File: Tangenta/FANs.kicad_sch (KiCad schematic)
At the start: 8 parts, among them M1 Fan_4pin, M2 Fan_4pin, Q3 BSS138

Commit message: Libraries exported from global to project.
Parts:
- M1, M2: symbol Motor:Fan_4pin -> CholaSymbolsPrjLib:Fan_4pin
- Q3: symbol Transistor_FET:BSS138 -> CholaSymbolsPrjLib:BSS138
- R2: symbol Device:R_Small_US -> CholaSymbolsPrjLib:R_Small_US
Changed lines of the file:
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@@
     (effects (font (size 1.27 1.27)) (justify right))
   )
-  (symbol (lib_id "Device:R_Small_US") (at 127 111.76 180) (unit 1)
+  (symbol (lib_id "CholaSymbolsPrjLib:R_Small_US") (at 127 111.76 180) (unit 1)
     (in_bom yes) (on_board yes) (dnp no)
     (property "Reference" "R2" (at 125.73 110.49 0)
@@
     )
   )
-  (symbol (lib_id "Device:R_Small_US") (at 127 78.105 180) (unit 1)
+  (symbol (lib_id "CholaSymbolsPrjLib:R_Small_US") (at 127 78.105 180) (unit 1)
     (in_bom yes) (on_board yes) (dnp no)
     (property "Reference" "R2" (at 125.73 76.835 0)
@@
     )
   )
-  (symbol (lib_id "Motor:Fan_4pin") (at 181.61 115.57 0) (unit 1)
+  (symbol (lib_id "CholaSymbolsPrjLib:Fan_4pin") (at 181.61 115.57 0) (unit 1)
     (in_bom yes) (on_board yes) (dnp no)
     (property "Reference" "M2" (at 185.42 114.3 0)
@@
     )
   )
-  (symbol (lib_id "Transistor_FET:BSS138") (at 139.7 115.57 270) (unit 1)
+  (symbol (lib_id "CholaSymbolsPrjLib:BSS138") (at 139.7 115.57 270) (unit 1)
     (in_bom yes) (on_board yes) (dnp no)
     (property "Reference" "Q3" (at 142.24 113.03 90)
@@
     )
   )
-  (symbol (lib_id "Device:R_Small_US") (at 153.67 111.76 180) (unit 1)
+  (symbol (lib_id "CholaSymbolsPrjLib:R_Small_US") (at 153.67 111.76 180) (unit 1)
     (in_bom yes) (on_board yes) (dnp no)
     (property "Reference" "R2" (at 152.4 110.49 0)
@@
     )
   )
-  (symbol (lib_id "Device:R_Small_US") (at 153.67 78.105 180) (unit 1)
+  (symbol (lib_id "CholaSymbolsPrjLib:R_Small_US") (at 153.67 78.105 180) (unit 1)
     (in_bom yes) (on_board yes) (dnp no)
     (property "Reference" "R2" (at 152.4 76.835 0)
@@
     )
   )
-  (symbol (lib_id "Motor:Fan_4pin") (at 181.61 81.915 0) (unit 1)
+  (symbol (lib_id "CholaSymbolsPrjLib:Fan_4pin") (at 181.61 81.915 0) (unit 1)
     (in_bom yes) (on_board yes) (dnp no)
     (property "Reference" "M1" (at 185.42 80.645 0)
@@
     )
   )
-  (symbol (lib_id "Transistor_FET:BSS138") (at 139.7 81.915 270) (unit 1)
+  (symbol (lib_id "CholaSymbolsPrjLib:BSS138") (at 139.7 81.915 270) (unit 1)
     (in_bom yes) (on_board yes) (dnp no)
     (property "Reference" "Q3" (at 142.24 79.375 90)

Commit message: initialize branch
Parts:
- renumbered Q3 to Q23, Q3 to Q24, R2 to R204, R2 to R205, R2 to R206, R2 to R207
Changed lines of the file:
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@@
   (symbol (lib_id "CholaSymbolsPrjLib:R_Small_US") (at 127 111.76 180) (unit 1)
     (in_bom yes) (on_board yes) (dnp no)
-    (property "Reference" "R2" (at 125.73 110.49 0)
+    (property "Reference" "R205" (at 125.73 110.49 0)
       (effects (font (size 1.27 1.27)) (justify left))
     )
@@
     (instances
       (project "Tangenta"
-        (path "/358d1bcf-7599-4352-8c4d-baa18a5f09e6/8215796b-9611-4f43-bcc5-319f8414b8a6"
-          (reference "R2") (unit 1)
-        )
-        (path "/358d1bcf-7599-4352-8c4d-baa18a5f09e6/d6c05402-162e-441f-bed8-be7996260fb4"
-          (reference "R18") (unit 1)
-        )
-        (path "/358d1bcf-7599-4352-8c4d-baa18a5f09e6/b1871a4d-6a35-44e2-a9a2-9a4af684371d"
-          (reference "R26") (unit 1)
-        )
-        (path "/358d1bcf-7599-4352-8c4d-baa18a5f09e6/6a8c68b5-4a7d-449e-86f6-34ced6d1cb55"
-          (reference "R41") (unit 1)
-        )
-        (path "/358d1bcf-7599-4352-8c4d-baa18a5f09e6/db297b0b-35f2-4e86-892c-83973f1ac2db"
-          (reference "R41") (unit 1)
-        )
-        (path "/358d1bcf-7599-4352-8c4d-baa18a5f09e6/98e3b24f-9927-4339-b8fd-9deea91a522a"
-          (reference "R158") (unit 1)
-        )
         (path "/358d1bcf-7599-4352-8c4d-baa18a5f09e6/19b4ac3b-c2a1-43b1-8d7b-1ca5ac2c79ee"
           (reference "R205") (unit 1)
@@
   (symbol (lib_id "CholaSymbolsPrjLib:R_Small_US") (at 127 78.105 180) (unit 1)
     (in_bom yes) (on_board yes) (dnp no)
-    (property "Reference" "R2" (at 125.73 76.835 0)
+    (property "Reference" "R204" (at 125.73 76.835 0)
       (effects (font (size 1.27 1.27)) (justify left))
     )
@@
     (instances
       (project "Tangenta"
-        (path "/358d1bcf-7599-4352-8c4d-baa18a5f09e6/8215796b-9611-4f43-bcc5-319f8414b8a6"
-          (reference "R2") (unit 1)
-        )
-        (path "/358d1bcf-7599-4352-8c4d-baa18a5f09e6/d6c05402-162e-441f-bed8-be7996260fb4"
-          (reference "R18") (unit 1)
-        )
-        (path "/358d1bcf-7599-4352-8c4d-baa18a5f09e6/b1871a4d-6a35-44e2-a9a2-9a4af684371d"
-          (reference "R26") (unit 1)
-        )
-        (path "/358d1bcf-7599-4352-8c4d-baa18a5f09e6/6a8c68b5-4a7d-449e-86f6-34ced6d1cb55"
-          (reference "R41") (unit 1)
-        )
-        (path "/358d1bcf-7599-4352-8c4d-baa18a5f09e6/db297b0b-35f2-4e86-892c-83973f1ac2db"
-          (reference "R41") (unit 1)
-        )
-        (path "/358d1bcf-7599-4352-8c4d-baa18a5f09e6/98e3b24f-9927-4339-b8fd-9deea91a522a"
-          (reference "R158") (unit 1)
-        )
         (path "/358d1bcf-7599-4352-8c4d-baa18a5f09e6/19b4ac3b-c2a1-43b1-8d7b-1ca5ac2c79ee"
           (reference "R204") (unit 1)
@@
   (symbol (lib_id "CholaSymbolsPrjLib:BSS138") (at 139.7 115.57 270) (unit 1)
     (in_bom yes) (on_board yes) (dnp no)
-    (property "Reference" "Q3" (at 142.24 113.03 90)
+    (property "Reference" "Q24" (at 142.24 113.03 90)
       (effects (font (size 1.27 1.27)))
     )
@@
     (instances
       (project "Tangenta"
-        (path "/358d1bcf-7599-4352-8c4d-baa18a5f09e6/6a8c68b5-4a7d-449e-86f6-34ced6d1cb55"
-          (reference "Q3") (unit 1)
-        )
-        (path "/358d1bcf-7599-4352-8c4d-baa18a5f09e6/db297b0b-35f2-4e86-892c-83973f1ac2db"
-          (reference "Q5") (unit 1)
-        )
-        (path "/358d1bcf-7599-4352-8c4d-baa18a5f09e6/98e3b24f-9927-4339-b8fd-9deea91a522a"
-          (reference "Q10") (unit 1)
-        )
         (path "/358d1bcf-7599-4352-8c4d-baa18a5f09e6/19b4ac3b-c2a1-43b1-8d7b-1ca5ac2c79ee"
           (reference "Q24") (unit 1)
@@
   (symbol (lib_id "CholaSymbolsPrjLib:R_Small_US") (at 153.67 111.76 180) (unit 1)
     (in_bom yes) (on_board yes) (dnp no)
-    (property "Reference" "R2" (at 152.4 110.49 0)
+    (property "Reference" "R207" (at 152.4 110.49 0)
       (effects (font (size 1.27 1.27)) (justify left))
     )
@@
     (instances
       (project "Tangenta"
-        (path "/358d1bcf-7599-4352-8c4d-baa18a5f09e6/8215796b-9611-4f43-bcc5-319f8414b8a6"
-          (reference "R2") (unit 1)
-        )
-        (path "/358d1bcf-7599-4352-8c4d-baa18a5f09e6/d6c05402-162e-441f-bed8-be7996260fb4"
-          (reference "R18") (unit 1)
-        )
-        (path "/358d1bcf-7599-4352-8c4d-baa18a5f09e6/b1871a4d-6a35-44e2-a9a2-9a4af684371d"
-          (reference "R28") (unit 1)
-        )
-        (path "/358d1bcf-7599-4352-8c4d-baa18a5f09e6/db297b0b-35f2-4e86-892c-83973f1ac2db"
-          (reference "R28") (unit 1)
-        )
-        (path "/358d1bcf-7599-4352-8c4d-baa18a5f09e6/98e3b24f-9927-4339-b8fd-9deea91a522a"
-          (reference "R159") (unit 1)
-        )
         (path "/358d1bcf-7599-4352-8c4d-baa18a5f09e6/19b4ac3b-c2a1-43b1-8d7b-1ca5ac2c79ee"
           (reference "R207") (unit 1)
@@
   (symbol (lib_id "CholaSymbolsPrjLib:R_Small_US") (at 153.67 78.105 180) (unit 1)
     (in_bom yes) (on_board yes) (dnp no)
-    (property "Reference" "R2" (at 152.4 76.835 0)
+    (property "Reference" "R206" (at 152.4 76.835 0)
       (effects (font (size 1.27 1.27)) (justify left))
     )
@@
     (instances
       (project "Tangenta"
-        (path "/358d1bcf-7599-4352-8c4d-baa18a5f09e6/8215796b-9611-4f43-bcc5-319f8414b8a6"
-          (reference "R2") (unit 1)
-        )
-        (path "/358d1bcf-7599-4352-8c4d-baa18a5f09e6/d6c05402-162e-441f-bed8-be7996260fb4"
-          (reference "R18") (unit 1)
-        )
-        (path "/358d1bcf-7599-4352-8c4d-baa18a5f09e6/b1871a4d-6a35-44e2-a9a2-9a4af684371d"
-          (reference "R28") (unit 1)
-        )
-        (path "/358d1bcf-7599-4352-8c4d-baa18a5f09e6/db297b0b-35f2-4e86-892c-83973f1ac2db"
-          (reference "R28") (unit 1)
-        )
-        (path "/358d1bcf-7599-4352-8c4d-baa18a5f09e6/98e3b24f-9927-4339-b8fd-9deea91a522a"
-          (reference "R159") (unit 1)
-        )
         (path "/358d1bcf-7599-4352-8c4d-baa18a5f09e6/19b4ac3b-c2a1-43b1-8d7b-1ca5ac2c79ee"
           (reference "R206") (unit 1)
@@
   (symbol (lib_id "power:GNDREF") (at 181.61 123.825 0) (unit 1)
     (in_bom yes) (on_board yes) (dnp no) (fields_autoplaced)
-    (property "Reference" "#PWR030" (at 181.61 130.175 0)
+    (property "Reference" "#PWR0112" (at 181.61 130.175 0)
       (effects (font (size 1.27 1.27)) hide)
     )
@@
     (instances
       (project "Tangenta"
-        (path "/358d1bcf-7599-4352-8c4d-baa18a5f09e6/b1871a4d-6a35-44e2-a9a2-9a4af684371d"
-          (reference "#PWR030") (unit 1)
-        )
-        (path "/358d1bcf-7599-4352-8c4d-baa18a5f09e6/f1c5822c-e7b8-40ae-bab0-71fd1c2cfc7c"
-          (reference "#PWR035") (unit 1)
-        )
-        (path "/358d1bcf-7599-4352-8c4d-baa18a5f09e6/98e3b24f-9927-4339-b8fd-9deea91a522a"
-          (reference "#PWR076") (unit 1)
-        )
         (path "/358d1bcf-7599-4352-8c4d-baa18a5f09e6/19b4ac3b-c2a1-43b1-8d7b-1ca5ac2c79ee"
           (reference "#PWR0112") (unit 1)
@@
   (symbol (lib_id "power:GNDREF") (at 181.61 90.17 0) (unit 1)
     (in_bom yes) (on_board yes) (dnp no) (fields_autoplaced)
-    (property "Reference" "#PWR030" (at 181.61 96.52 0)
+    (property "Reference" "#PWR0111" (at 181.61 96.52 0)
       (effects (font (size 1.27 1.27)) hide)
     )
@@
     (instances
       (project "Tangenta"
-        (path "/358d1bcf-7599-4352-8c4d-baa18a5f09e6/b1871a4d-6a35-44e2-a9a2-9a4af684371d"
-          (reference "#PWR030") (unit 1)
-        )
-        (path "/358d1bcf-7599-4352-8c4d-baa18a5f09e6/f1c5822c-e7b8-40ae-bab0-71fd1c2cfc7c"
-          (reference "#PWR035") (unit 1)
-        )
-        (path "/358d1bcf-7599-4352-8c4d-baa18a5f09e6/98e3b24f-9927-4339-b8fd-9deea91a522a"
-          (reference "#PWR076") (unit 1)
-        )
         (path "/358d1bcf-7599-4352-8c4d-baa18a5f09e6/19b4ac3b-c2a1-43b1-8d7b-1ca5ac2c79ee"
           (reference "#PWR0111") (unit 1)
@@
   (symbol (lib_id "CholaSymbolsPrjLib:BSS138") (at 139.7 81.915 270) (unit 1)
     (in_bom yes) (on_board yes) (dnp no)
-    (property "Reference" "Q3" (at 142.24 79.375 90)
+    (property "Reference" "Q23" (at 142.24 79.375 90)
       (effects (font (size 1.27 1.27)))
     )
@@
     (instances
       (project "Tangenta"
-        (path "/358d1bcf-7599-4352-8c4d-baa18a5f09e6/6a8c68b5-4a7d-449e-86f6-34ced6d1cb55"
-          (reference "Q3") (unit 1)
-        )
-        (path "/358d1bcf-7599-4352-8c4d-baa18a5f09e6/db297b0b-35f2-4e86-892c-83973f1ac2db"
-          (reference "Q5") (unit 1)
-        )
-        (path "/358d1bcf-7599-4352-8c4d-baa18a5f09e6/98e3b24f-9927-4339-b8fd-9deea91a522a"
-          (reference "Q10") (unit 1)
-        )
         (path "/358d1bcf-7599-4352-8c4d-baa18a5f09e6/19b4ac3b-c2a1-43b1-8d7b-1ca5ac2c79ee"
           (reference "Q23") (unit 1)
@@
   (symbol (lib_id "power:GNDREF") (at 43.18 25.4 90) (unit 1)
     (in_bom yes) (on_board yes) (dnp no) (fields_autoplaced)
-    (property "Reference" "#PWR030" (at 49.53 25.4 0)
+    (property "Reference" "#PWR0110" (at 49.53 25.4 0)
       (effects (font (size 1.27 1.27)) hide)
     )
@@
     (instances
       (project "Tangenta"
-        (path "/358d1bcf-7599-4352-8c4d-baa18a5f09e6/b1871a4d-6a35-44e2-a9a2-9a4af684371d"
-          (reference "#PWR030") (unit 1)
-        )
-        (path "/358d1bcf-7599-4352-8c4d-baa18a5f09e6/f1c5822c-e7b8-40ae-bab0-71fd1c2cfc7c"
-          (reference "#PWR035") (unit 1)
-        )
-        (path "/358d1bcf-7599-4352-8c4d-baa18a5f09e6/98e3b24f-9927-4339-b8fd-9deea91a522a"
-          (reference "#PWR076") (unit 1)
-        )
         (path "/358d1bcf-7599-4352-8c4d-baa18a5f09e6/19b4ac3b-c2a1-43b1-8d7b-1ca5ac2c79ee"
           (reference "#PWR0110") (unit 1)

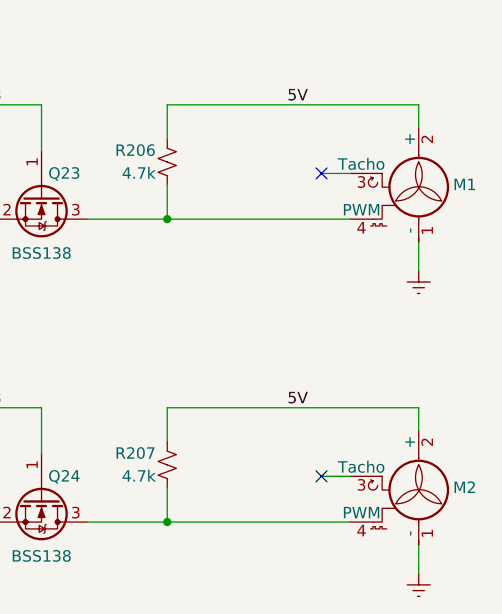
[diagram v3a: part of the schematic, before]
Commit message: Saved in KiCAD9, ERC and DRC pass.
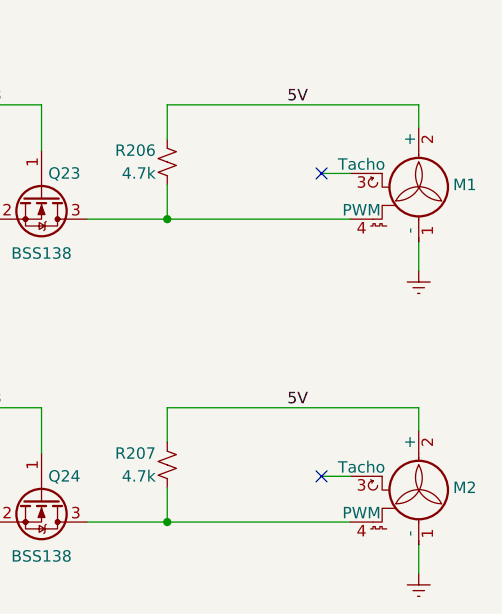
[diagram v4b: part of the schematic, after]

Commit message: Removing component association with previous project (local) libraries.
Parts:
- M1, M2: symbol CholaSymbolsPrjLib:Fan_4pin -> Fan_4pin:Fan_4pin
- Q23, Q24: symbol CholaSymbolsPrjLib:BSS138 -> BSS138:BSS138
- R204, R205, R206, R207: symbol CholaSymbolsPrjLib:R_Small_US -> R_Small_US:R_Small_US
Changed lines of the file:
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@@
 	)
 	(symbol
-		(lib_id "CholaSymbolsPrjLib:R_Small_US")
+		(lib_id "R_Small_US:R_Small_US")
 		(at 127 111.76 180)
 		(unit 1)
@@
 	)
 	(symbol
-		(lib_id "CholaSymbolsPrjLib:R_Small_US")
+		(lib_id "R_Small_US:R_Small_US")
 		(at 127 78.105 180)
 		(unit 1)
@@
 	)
 	(symbol
-		(lib_id "CholaSymbolsPrjLib:Fan_4pin")
+		(lib_id "Fan_4pin:Fan_4pin")
 		(at 181.61 115.57 0)
 		(unit 1)
@@
 	)
 	(symbol
-		(lib_id "CholaSymbolsPrjLib:BSS138")
+		(lib_id "BSS138:BSS138")
 		(at 139.7 115.57 270)
 		(unit 1)
@@
 	)
 	(symbol
-		(lib_id "CholaSymbolsPrjLib:R_Small_US")
+		(lib_id "R_Small_US:R_Small_US")
 		(at 153.67 111.76 180)
 		(unit 1)
@@
 	)
 	(symbol
-		(lib_id "CholaSymbolsPrjLib:R_Small_US")
+		(lib_id "R_Small_US:R_Small_US")
 		(at 153.67 78.105 180)
 		(unit 1)
@@
 	)
 	(symbol
-		(lib_id "CholaSymbolsPrjLib:Fan_4pin")
+		(lib_id "Fan_4pin:Fan_4pin")
 		(at 181.61 81.915 0)
 		(unit 1)
@@
 	)
 	(symbol
-		(lib_id "CholaSymbolsPrjLib:BSS138")
+		(lib_id "BSS138:BSS138")
 		(at 139.7 81.915 270)
 		(unit 1)

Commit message: Fixes, before checks.
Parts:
- M1, M2: symbol Fan_4pin:Fan_4pin -> Motor:Fan_4pin
- Q23, Q24: symbol BSS138:BSS138 -> Transistor_FET:BSS138
- R204, R205, R206, R207: symbol R_Small_US:R_Small_US -> Device:R_Small_US
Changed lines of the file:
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@@
 	)
 	(symbol
-		(lib_id "R_Small_US:R_Small_US")
+		(lib_id "Device:R_Small_US")
 		(at 127 111.76 180)
 		(unit 1)
@@
 	)
 	(symbol
-		(lib_id "R_Small_US:R_Small_US")
+		(lib_id "Device:R_Small_US")
 		(at 127 78.105 180)
 		(unit 1)
@@
 	)
 	(symbol
-		(lib_id "Fan_4pin:Fan_4pin")
+		(lib_id "Motor:Fan_4pin")
 		(at 181.61 115.57 0)
 		(unit 1)
@@
 	)
 	(symbol
-		(lib_id "BSS138:BSS138")
+		(lib_id "Transistor_FET:BSS138")
 		(at 139.7 115.57 270)
 		(unit 1)
@@
 	)
 	(symbol
-		(lib_id "R_Small_US:R_Small_US")
+		(lib_id "Device:R_Small_US")
 		(at 153.67 111.76 180)
 		(unit 1)
@@
 	)
 	(symbol
-		(lib_id "R_Small_US:R_Small_US")
+		(lib_id "Device:R_Small_US")
 		(at 153.67 78.105 180)
 		(unit 1)
@@
 	)
 	(symbol
-		(lib_id "Fan_4pin:Fan_4pin")
+		(lib_id "Motor:Fan_4pin")
 		(at 181.61 81.915 0)
 		(unit 1)
@@
 	)
 	(symbol
-		(lib_id "BSS138:BSS138")
+		(lib_id "Transistor_FET:BSS138")
 		(at 139.7 81.915 270)
 		(unit 1)

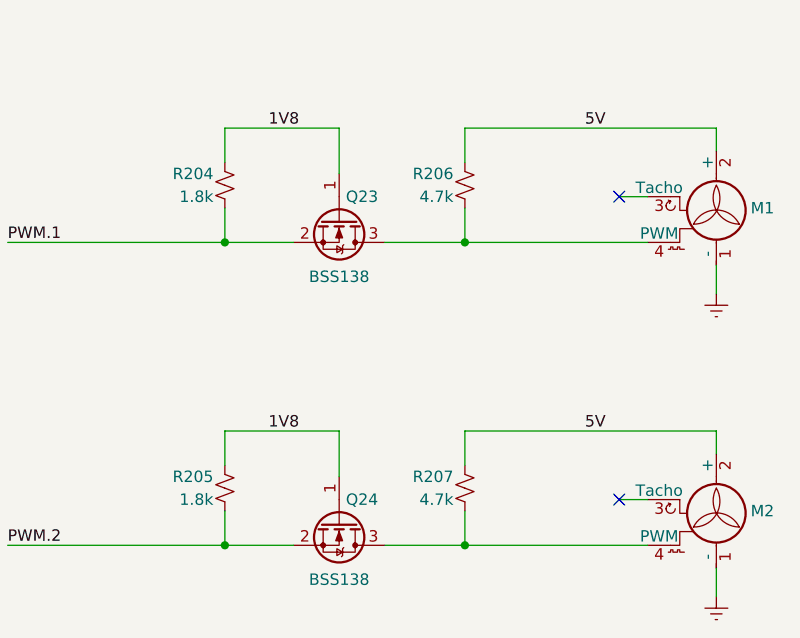
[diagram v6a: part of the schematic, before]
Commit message: Reverting to the original design.
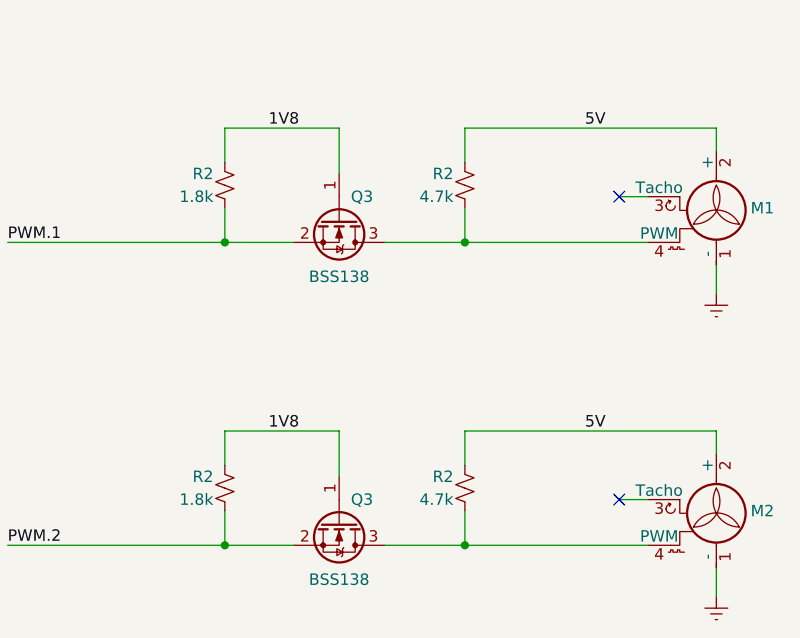
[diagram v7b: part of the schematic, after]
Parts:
- M1, M2: symbol Motor:Fan_4pin -> CholaSymbolsPrjLib:Fan_4pin
- Q3: renamed from Q24; symbol Transistor_FET:BSS138 -> CholaSymbolsPrjLib:BSS138
- Q3: renamed from Q23; symbol Transistor_FET:BSS138 -> CholaSymbolsPrjLib:BSS138
- R2: renamed from R205; symbol Device:R_Small_US -> CholaSymbolsPrjLib:R_Small_US
- R2: renamed from R204; symbol Device:R_Small_US -> CholaSymbolsPrjLib:R_Small_US
- R2: renamed from R207; symbol Device:R_Small_US -> CholaSymbolsPrjLib:R_Small_US
- R2: renamed from R206; symbol Device:R_Small_US -> CholaSymbolsPrjLib:R_Small_US

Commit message: ...
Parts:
- M1, M2: symbol CholaSymbolsPrjLib:Fan_4pin -> LocalPrjLib:Fan_4pin
- Q3: symbol CholaSymbolsPrjLib:BSS138 -> LocalPrjLib:BSS138
- R2: symbol CholaSymbolsPrjLib:R_Small_US -> LocalPrjLib:R_Small_US
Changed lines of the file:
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@@
     (effects (font (size 1.27 1.27)) (justify right))
   )
-  (symbol (lib_id "CholaSymbolsPrjLib:R_Small_US") (at 127 111.76 180) (unit 1)
+  (symbol (lib_id "LocalPrjLib:R_Small_US") (at 127 111.76 180) (unit 1)
     (in_bom yes) (on_board yes) (dnp no)
     (property "Reference" "R2" (at 125.73 110.49 0)
@@
     )
   )
-  (symbol (lib_id "CholaSymbolsPrjLib:R_Small_US") (at 127 78.105 180) (unit 1)
+  (symbol (lib_id "LocalPrjLib:R_Small_US") (at 127 78.105 180) (unit 1)
     (in_bom yes) (on_board yes) (dnp no)
     (property "Reference" "R2" (at 125.73 76.835 0)
@@
     )
   )
-  (symbol (lib_id "CholaSymbolsPrjLib:Fan_4pin") (at 181.61 115.57 0) (unit 1)
+  (symbol (lib_id "LocalPrjLib:Fan_4pin") (at 181.61 115.57 0) (unit 1)
     (in_bom yes) (on_board yes) (dnp no)
     (property "Reference" "M2" (at 185.42 114.3 0)
@@
     )
   )
-  (symbol (lib_id "CholaSymbolsPrjLib:BSS138") (at 139.7 115.57 270) (unit 1)
+  (symbol (lib_id "LocalPrjLib:BSS138") (at 139.7 115.57 270) (unit 1)
     (in_bom yes) (on_board yes) (dnp no)
     (property "Reference" "Q3" (at 142.24 113.03 90)
@@
     )
   )
-  (symbol (lib_id "CholaSymbolsPrjLib:R_Small_US") (at 153.67 111.76 180) (unit 1)
+  (symbol (lib_id "LocalPrjLib:R_Small_US") (at 153.67 111.76 180) (unit 1)
     (in_bom yes) (on_board yes) (dnp no)
     (property "Reference" "R2" (at 152.4 110.49 0)
@@
     )
   )
-  (symbol (lib_id "CholaSymbolsPrjLib:R_Small_US") (at 153.67 78.105 180) (unit 1)
+  (symbol (lib_id "LocalPrjLib:R_Small_US") (at 153.67 78.105 180) (unit 1)
     (in_bom yes) (on_board yes) (dnp no)
     (property "Reference" "R2" (at 152.4 76.835 0)
@@
     )
   )
-  (symbol (lib_id "CholaSymbolsPrjLib:Fan_4pin") (at 181.61 81.915 0) (unit 1)
+  (symbol (lib_id "LocalPrjLib:Fan_4pin") (at 181.61 81.915 0) (unit 1)
     (in_bom yes) (on_board yes) (dnp no)
     (property "Reference" "M1" (at 185.42 80.645 0)
@@
     )
   )
-  (symbol (lib_id "CholaSymbolsPrjLib:BSS138") (at 139.7 81.915 270) (unit 1)
+  (symbol (lib_id "LocalPrjLib:BSS138") (at 139.7 81.915 270) (unit 1)
     (in_bom yes) (on_board yes) (dnp no)
     (property "Reference" "Q3" (at 142.24 79.375 90)
